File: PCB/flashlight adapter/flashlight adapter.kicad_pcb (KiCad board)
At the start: 2 copper layers, 30.1 x 28.9 mm, 38 parts, among them J1 USB4105-GF-A, Q1 FS8205A, Q2 Q_NMOS_GSD, U1 BQ24074RGT, U2 DW01A, U3 MIC2295YD5-TR

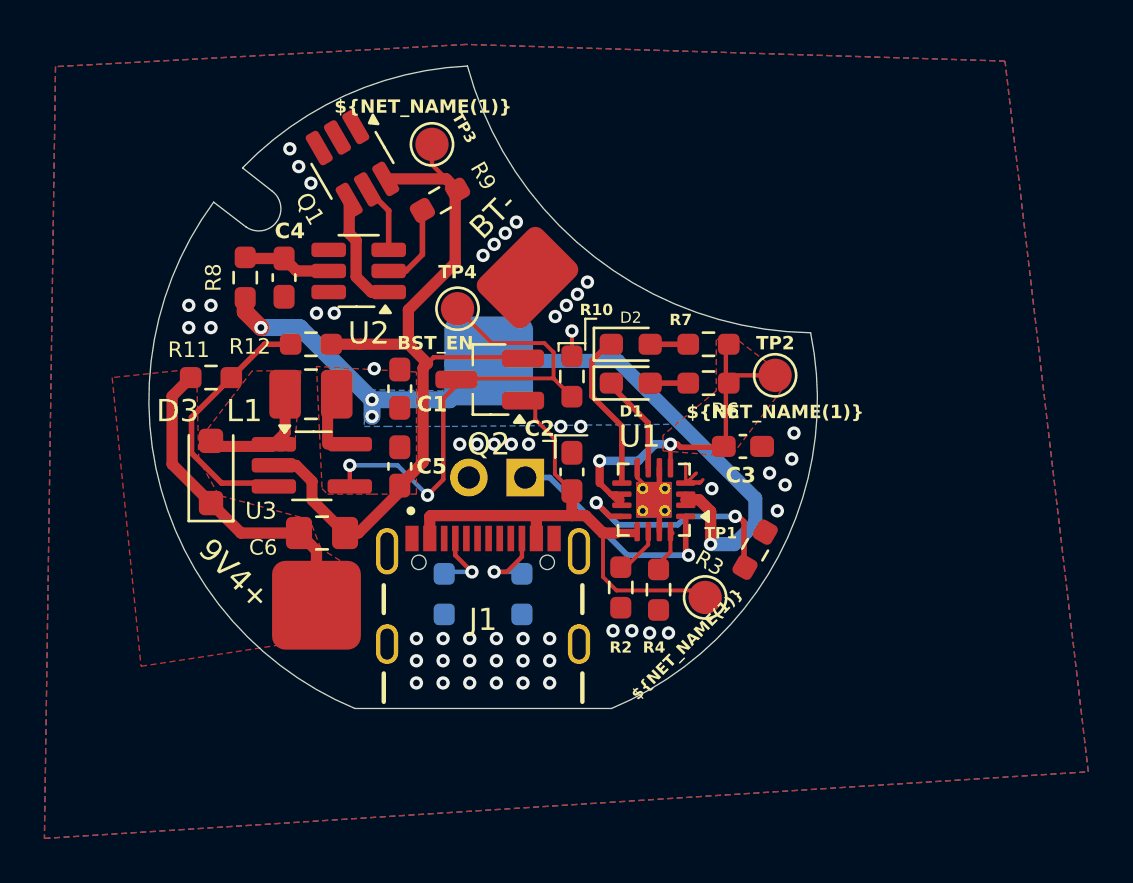
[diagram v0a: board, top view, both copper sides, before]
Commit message: Fixed usb switch mosfet footprint, sent out second order
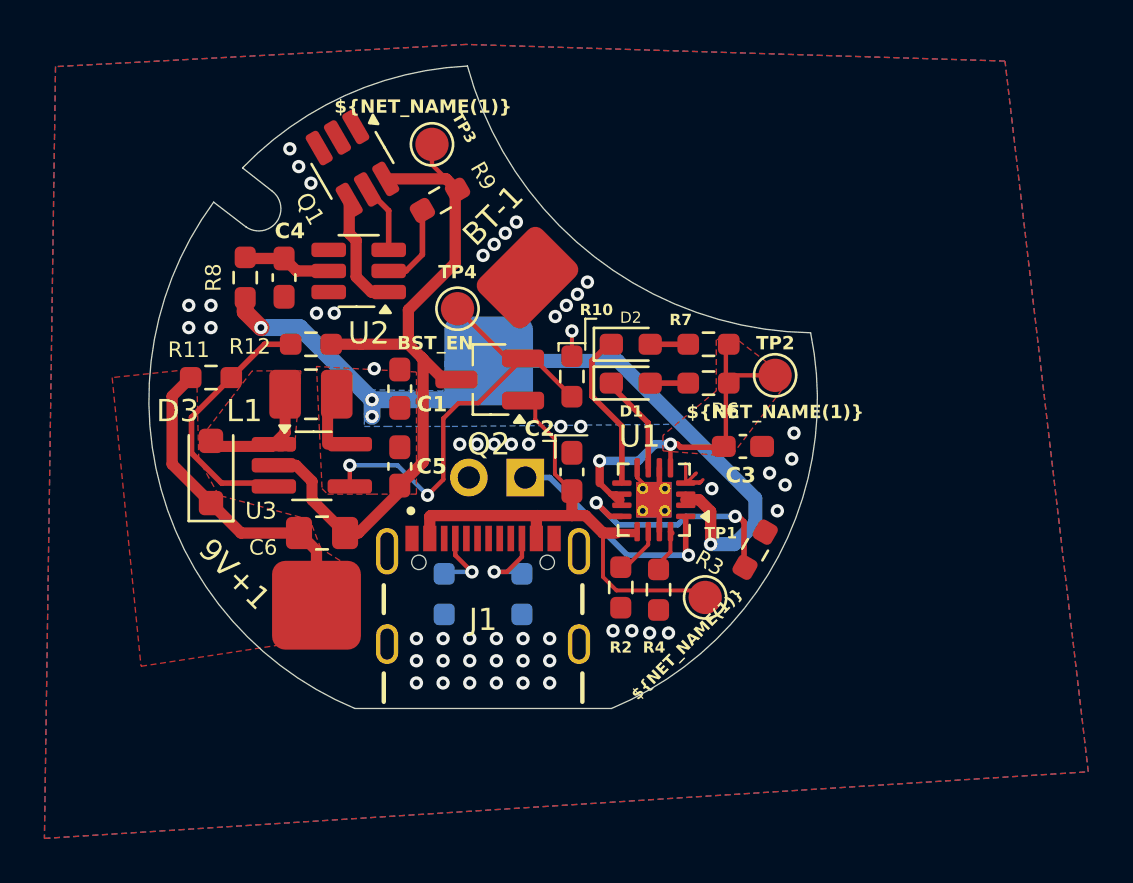
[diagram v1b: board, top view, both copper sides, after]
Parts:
- renumbered 9V4+ to 9V+1, BT- to BT-1
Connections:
- Q2 pad 2: /P- -> Net-(Q2-S)
- Q2 pad 3: Net-(Q2-D) -> /P-
- R10 pad 2: Net-(Q2-D) -> Net-(Q2-S)
- TP4 pad 1: Net-(Q2-D) -> Net-(Q2-S)
- U3 pad 4: Net-(Q2-D) -> Net-(Q2-S)
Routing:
- net Net-(Q2-D): track 22.8 -> 0.00 mm, vias 2 -> 0
- net Net-(Q2-S): track 0.00 -> 20.5 mm, vias 0 -> 2
- net /P-: track 37.2 -> 34.3 mm
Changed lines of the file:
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@@
 			(drillshape 0)
 			(scaleselection 1)
-			(outputdirectory "Exports/")
+			(outputdirectory "Exports/V1.1/")
 		)
 	)
@@
 	(net 28 "unconnected-(Q1-Pad1)")
 	(net 29 "Net-(U2-OC)")
-	(net 30 "Net-(Q2-D)")
+	(net 30 "Net-(Q2-S)")
 	(net 31 "/P-")
 	(footprint "LED_SMD:LED_0603_1608Metric_Pad1.05x0.95mm_HandSolder"
@@
 			(layers "F.Cu" "F.Mask" "F.Paste")
 			(roundrect_rratio 0.25)
-			(net 30 "Net-(Q2-D)")
+			(net 30 "Net-(Q2-S)")
 			(pinfunction "EN")
 			(pintype "input")
@@
 			(layers "F.Cu" "F.Mask" "F.Paste")
 			(roundrect_rratio 0.25)
-			(net 30 "Net-(Q2-D)")
+			(net 30 "Net-(Q2-S)")
 			(pintype "passive")
 		)
@@
 			)
 		)
-		(property "Datasheet" "https://www.digikey.com/en/products/detail/diodes-incorporated/BSS138K-7-W/27803573"
+		(property "Datasheet" "~"
 			(at 0 0 180)
 			(unlocked yes)
@@
 			)
 		)
-		(property "Description" "N-MOSFET transistor, gate/source/drain"
+		(property "Description" "N-MOSFET transistor, gate/drain/source"
 			(at 0 0 180)
 			(unlocked yes)
@@
 			(layers "F.Cu" "F.Mask" "F.Paste")
 			(roundrect_rratio 0.25)
-			(net 31 "/P-")
-			(pinfunction "S")
+			(net 30 "Net-(Q2-S)")
+			(pinfunction "D")
 			(pintype "passive")
 		)
@@
 			(layers "F.Cu" "F.Mask" "F.Paste")
 			(roundrect_rratio 0.25)
-			(net 30 "Net-(Q2-D)")
-			(pinfunction "D")
+			(net 31 "/P-")
+			(pinfunction "S")
 			(pintype "passive")
 		)
@@
 		(layer "F.Cu")
 		(at 138 102.75)
-		(property "Reference" "9V4+"
+		(property "Reference" "9V+1"
 			(at -3.7 -1.4 315)
 			(unlocked yes)
@@
 			(size 1.5 1.5)
 			(layers "F.Cu" "F.Mask")
-			(net 30 "Net-(Q2-D)")
+			(net 30 "Net-(Q2-S)")
 			(pinfunction "1")
 			(pintype "passive")
@@
 		(layer "F.Cu")
 		(at 147.5 88 90)
-		(property "Reference" "BT-"
+		(property "Reference" "BT-1"
 			(at 2.8 -1.55 45)
 			(unlocked yes)
@@
 	)
 	(segment
-		(start 145.8976 90.9476)
-		(end 148.258466 90.9476)
-		(width 0.1778)
+		(start 147.6875 91.55)
+		(end 149.5 93.3625)
+		(width 0.2)
 		(layer "F.Cu")
 		(net 30)
 	)
 	(segment
-		(start 143.709 93.441)
-		(end 144.6125 92.5375)
+		(start 143.709 94.341)
+		(end 144.4 93.65)
 		(width 0.2)
 		(layer "F.Cu")
@@
 	)
 	(segment
-		(start 144.6125 92.5375)
-		(end 144.85 92.5375)
+		(start 144.4 93.65)
+		(end 145.2875 93.65)
 		(width 0.2)
 		(layer "F.Cu")
@@
 	)
 	(segment
-		(start 144.35 89.4)
-		(end 145.8976 90.9476)
-		(width 0.1778)
+		(start 147.25 91.55)
+		(end 147.6875 91.55)
+		(width 0.2)
 		(layer "F.Cu")
 		(net 30)
 	)
 	(segment
-		(start 149.5 93.3625)
-		(end 148.675 92.5375)
-		(width 0.1778)
+		(start 143.709 97.091)
+		(end 143.709 94.341)
+		(width 0.2)
 		(layer "F.Cu")
 		(net 30)
 	)
 	(segment
-		(start 143 97.8)
-		(end 143.709 97.091)
+		(start 147.3 91.6)
+		(end 147.25 91.55)
 		(width 0.2)
 		(layer "F.Cu")
@@
 	)
 	(segment
-		(start 148.675 92.5375)
-		(end 144.55 92.5375)
-		(width 0.1778)
+		(start 146.5875 91.6375)
+		(end 147.3 91.6375)
+		(width 0.2032)
 		(layer "F.Cu")
 		(net 30)
 	)
 	(segment
-		(start 139.5 97.4)
-		(end 139.5 96.45)
+		(start 145.2875 93.65)
+		(end 147.3 91.6375)
 		(width 0.2)
 		(layer "F.Cu")
@@
 	)
 	(segment
-		(start 148.675 91.364134)
-		(end 148.675 92.5375)
-		(width 0.1778)
+		(start 144.35 89.4)
+		(end 146.5875 91.6375)
+		(width 0.2032)
 		(layer "F.Cu")
 		(net 30)
 	)
 	(segment
-		(start 143.709 97.091)
-		(end 143.709 93.441)
+		(start 139.5 97.4)
+		(end 139.5 96.45)
 		(width 0.2)
 		(layer "F.Cu")
@@
 	)
 	(segment
-		(start 148.258466 90.9476)
-		(end 148.675 91.364134)
-		(width 0.1778)
+		(start 143 97.8)
+		(end 143.709 97.091)
+		(width 0.2)
+		(layer "F.Cu")
+		(net 30)
+	)
+	(segment
+		(start 147.3 91.6375)
+		(end 147.3 91.6)
+		(width 0.2)
 		(layer "F.Cu")
 		(net 30)
@@
 	)
 	(segment
-		(start 147.85 91.5875)
-		(end 143.276576 91.5875)
-		(width 0.2)
-		(layer "F.Cu")
-		(net 31)
-	)
-	(segment
-		(start 142.8 92.064076)
+		(start 142.8 91.664076)
 		(end 142.8 96.3125)
 		(width 0.508)
@@
 	)
 	(segment
+		(start 144.3 92.5875)
+		(end 143.723424 92.5875)
+		(width 0.2)
+		(layer "F.Cu")
+		(net 31)
+	)
+	(segment
 		(start 137.079999 96.45)
 		(end 137.799 97.169001)
@@
 	)
 	(segment
+		(start 143.723424 92.5875)
+		(end 142.717962 91.582038)
+		(width 0.508)
+		(layer "F.Cu")
+		(net 31)
+	)
+	(segment
 		(start 143.840633 83.554134)
 		(end 141.117724 83.554134)
@@
 	)
 	(segment
+		(start 144.6125 92.5375)
+		(end 144.85 92.5375)
+		(width 0.2)
+		(layer "F.Cu")
+		(net 31)
+	)
+	(segment
 		(start 136.08 96.45)
 		(end 137.079999 96.45)
@@
 	)
 	(segment
-		(start 142.8 96.3125)
-		(end 141.75 97.3625)
-		(width 0.508)
-		(layer "F.Cu")
-		(net 31)
-	)
-	(segment
-		(start 143 91.864076)
-		(end 142.8 92.064076)
+		(start 142.717962 91.582038)
+		(end 142.8 91.664076)
 		(width 0.508)
 		(layer "F.Cu")
@@
 	(segment
 		(start 142.135924 91)
-		(end 143 91.864076)
+		(end 142.717962 91.582038)
 		(width 0.508)
 		(layer "F.Cu")
@@
 	)
 	(segment
-		(start 143.276576 91.5875)
-		(end 143 91.864076)
-		(width 0.2)
+		(start 142.8 96.3125)
+		(end 141.75 97.3625)
+		(width 0.508)
 		(layer "F.Cu")
 		(net 31)

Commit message: Adjusted Silkscreen to say v1.1
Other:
- board text added: "9V li-ion flashlight Adapter V1.1 Made with <3 by Siwen Long"
- board text removed: "9V li-ion flashlight Adapter V1 Made with <3 by Siwen Long"
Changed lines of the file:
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@@
 		(layer "Edge.Cuts")
 	)
-	(gr_text "9V li-ion flashlight Adapter V1\nMade with <3 by\nSiwen Long"
-		(at 138.7 104.8 315)
+	(gr_text "9V li-ion flashlight Adapter V1.1\nMade with <3 by\nSiwen Long"
+		(at 138.9 105.2 315)
 		(layer "B.SilkS")
 		(effects
